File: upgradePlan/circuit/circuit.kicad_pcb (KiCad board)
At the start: 2 copper layers, 120 x 110 mm, 31 parts, among them J1 Connector_GY_521, J2 Conn_VL53L0/1xV2, J3 Conn_HC_SR04, M1 Motor_DC, M2 Motor_Servo, Q1 C945, Q2 C945, Q4 C945, SW2 SW_DPDT_x2, U1 Freenove-SP32-WROVER, U2 L293D, U3 LM350_TO220, U4 LM350_TO220, U5 LM317_TO-220

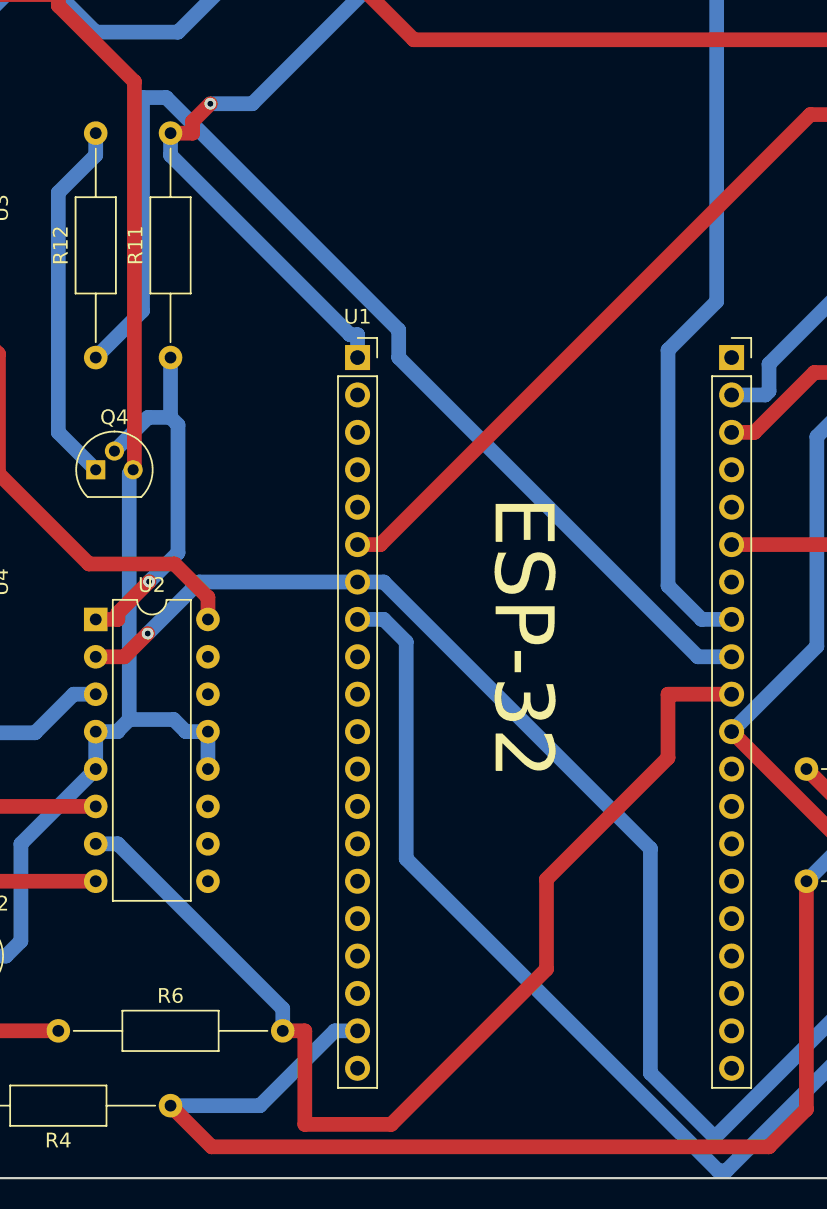
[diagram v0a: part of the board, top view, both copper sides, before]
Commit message: FIxed wrong copnnection in pcb and updated code correspondingly. Switch pin 31 and 30.
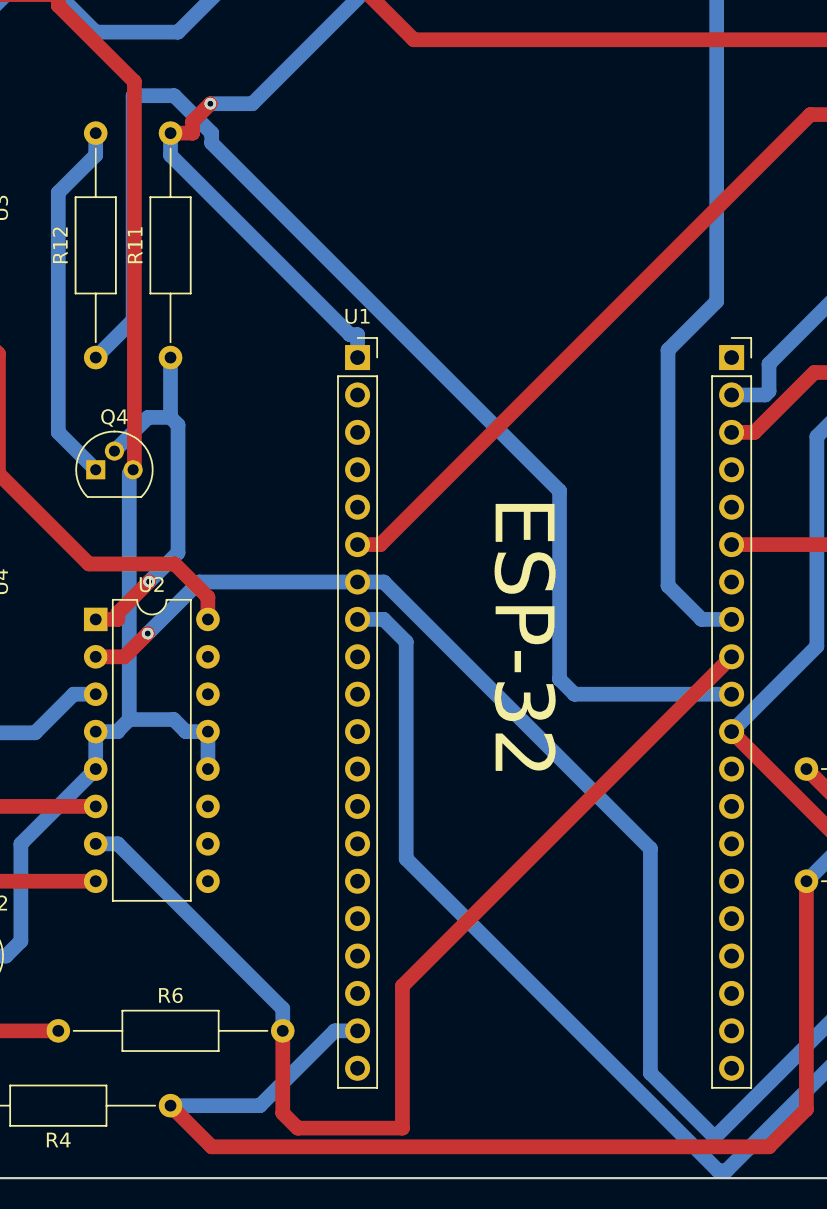
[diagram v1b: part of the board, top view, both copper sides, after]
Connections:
- R12 pad 1: Net-(U1-18) -> Net-(U1-5)
- R6 pad 2: Net-(U1-5) -> Net-(U1-18)
- U2 pad 7: Net-(U1-5) -> Net-(U1-18)
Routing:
- net Net-(U1-5): track 73.9 -> 84.2 mm
- net Net-(U1-18): track 75.8 -> 74.2 mm
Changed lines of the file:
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@@
       (net 6 "Net-(M1--)") (pinfunction "2Y") (pintype "output"))
     (pad "7" thru_hole oval (at 0 15.24) (size 1.6 1.6) (drill 0.8) (layers "*.Cu" "*.Mask")
-      (net 7 "Net-(U1-5)") (pinfunction "2A") (pintype "input"))
+      (net 38 "Net-(U1-18)") (pinfunction "2A") (pintype "input"))
     (pad "8" thru_hole oval (at 0 17.78) (size 1.6 1.6) (drill 0.8) (layers "*.Cu" "*.Mask")
       (net 5 "/MotorDrive") (pinfunction "VCC2") (pintype "power_in"))
@@
       (stroke (width 0.1) (type solid)) (layer "F.Fab"))
     (pad "1" thru_hole circle (at 0 0 90) (size 1.6 1.6) (drill 0.8) (layers "*.Cu" "*.Mask")
-      (net 38 "Net-(U1-18)") (pintype "passive"))
+      (net 7 "Net-(U1-5)") (pintype "passive"))
     (pad "2" thru_hole oval (at 15.24 0 90) (size 1.6 1.6) (drill 0.8) (layers "*.Cu" "*.Mask")
       (net 37 "Net-(Q4-B)") (pintype "passive"))
@@
       (net 36 "Net-(Q2-B)") (pintype "passive"))
     (pad "2" thru_hole oval (at 15.24 0) (size 1.6 1.6) (drill 0.8) (layers "*.Cu" "*.Mask")
-      (net 7 "Net-(U1-5)") (pintype "passive"))
+      (net 38 "Net-(U1-18)") (pintype "passive"))
     (model "${KICAD6_3DMODEL_DIR}/Resistor_THT.3dshapes/R_Axial_DIN0207_L6.3mm_D2.5mm_P15.24mm_Horizontal.wrl"
       (offset (xyz 0 0 0))
@@
   (segment (start 83.24 121.92) (end 91.44 121.92) (width 1) (layer "F.Cu") (net 6))
   (segment (start 91.44 121.92) (end 109.22 121.92) (width 1) (layer "F.Cu") (net 6))
-  (segment (start 148.082 114.3) (end 152.4 114.3) (width 1) (layer "F.Cu") (net 7))
-  (segment (start 123.4203 137.16) (end 123.4203 143.51) (width 1) (layer "F.Cu") (net 7))
-  (segment (start 121.92 137.16) (end 123.4203 137.16) (width 1) (layer "F.Cu") (net 7))
-  (segment (start 129.286 143.51) (end 139.8287 132.9673) (width 1) (layer "F.Cu") (net 7))
-  (segment (start 148.082 118.618) (end 148.082 114.3) (width 1) (layer "F.Cu") (net 7))
-  (segment (start 123.4203 143.51) (end 129.286 143.51) (width 1) (layer "F.Cu") (net 7))
-  (segment (start 139.8287 132.9673) (end 139.8287 126.8713) (width 1) (layer "F.Cu") (net 7))
-  (segment (start 139.8287 126.8713) (end 148.082 118.618) (width 1) (layer "F.Cu") (net 7))
-  (segment (start 121.92 137.16) (end 121.92 135.6597) (width 1) (layer "B.Cu") (net 7))
-  (segment (start 109.22 124.46) (end 110.7203 124.46) (width 1) (layer "B.Cu") (net 7))
-  (segment (start 110.7203 124.46) (end 121.92 135.6597) (width 1) (layer "B.Cu") (net 7))
+  (segment (start 111.76 88.9) (end 109.22 91.44) (width 1) (layer "B.Cu") (net 7))
+  (segment (start 140.716 113.284) (end 140.716 100.494679) (width 1) (layer "B.Cu") (net 7))
+  (segment (start 141.732 114.3) (end 140.716 113.284) (width 1) (layer "B.Cu") (net 7))
+  (segment (start 140.716 100.494679) (end 117.094 76.872679) (width 1) (layer "B.Cu") (net 7))
+  (segment (start 117.094 76.2) (end 114.554 73.66) (width 1) (layer "B.Cu") (net 7))
+  (segment (start 152.4 114.3) (end 141.732 114.3) (width 1) (layer "B.Cu") (net 7))
+  (segment (start 111.76 73.66) (end 111.76 88.9) (width 1) (layer "B.Cu") (net 7))
+  (segment (start 114.554 73.66) (end 111.76 73.66) (width 1) (layer "B.Cu") (net 7))
+  (segment (start 117.094 76.872679) (end 117.094 76.2) (width 1) (layer "B.Cu") (net 7))
   (segment (start 102.616 91.186) (end 92.71 81.28) (width 1) (layer "F.Cu") (net 8))
   (segment (start 116.84 107.7197) (end 114.5755 105.4552) (width 1) (layer "F.Cu") (net 8))
@@
   (segment (start 106.68 80.2403) (end 106.68 96.52) (width 1) (layer "B.Cu") (net 37))
   (segment (start 109.22 77.7003) (end 106.68 80.2403) (width 1) (layer "B.Cu") (net 37))
-  (segment (start 129.794 89.572679) (end 129.794 91.44) (width 1) (layer "B.Cu") (net 38))
-  (segment (start 114.006821 73.7855) (end 129.794 89.572679) (width 1) (layer "B.Cu") (net 38))
-  (segment (start 109.22 91.44) (end 112.3965 88.2635) (width 1) (layer "B.Cu") (net 38))
-  (segment (start 129.794 91.44) (end 150.114 111.76) (width 1) (layer "B.Cu") (net 38))
-  (segment (start 150.114 111.76) (end 152.4 111.76) (width 1) (layer "B.Cu") (net 38))
-  (segment (start 112.3965 88.2635) (end 112.3965 73.7855) (width 1) (layer "B.Cu") (net 38))
-  (segment (start 112.3965 73.7855) (end 114.006821 73.7855) (width 1) (layer "B.Cu") (net 38))
+  (segment (start 121.92 142.748) (end 121.92 137.16) (width 1) (layer "F.Cu") (net 38))
+  (segment (start 152.4 111.76) (end 130.048 134.112) (width 1) (layer "F.Cu") (net 38))
+  (segment (start 122.936 143.764) (end 121.92 142.748) (width 1) (layer "F.Cu") (net 38))
+  (segment (start 130.048 134.112) (end 130.048 143.764) (width 1) (layer "F.Cu") (net 38))
+  (segment (start 130.048 143.764) (end 122.936 143.764) (width 1) (layer "F.Cu") (net 38))
+  (segment (start 121.92 137.16) (end 121.92 135.6597) (width 1) (layer "B.Cu") (net 38))
+  (segment (start 109.22 124.46) (end 110.7203 124.46) (width 1) (layer "B.Cu") (net 38))
+  (segment (start 110.7203 124.46) (end 121.92 135.6597) (width 1) (layer "B.Cu") (net 38))
   (segment (start 87.376 58.42) (end 82.21 58.42) (width 1) (layer "F.Cu") (net 39))
   (segment (start 107.22 46.99) (end 98.806 46.99) (width 1) (layer "F.Cu") (net 39))
